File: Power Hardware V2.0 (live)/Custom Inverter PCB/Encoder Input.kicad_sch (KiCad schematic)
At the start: 0 parts

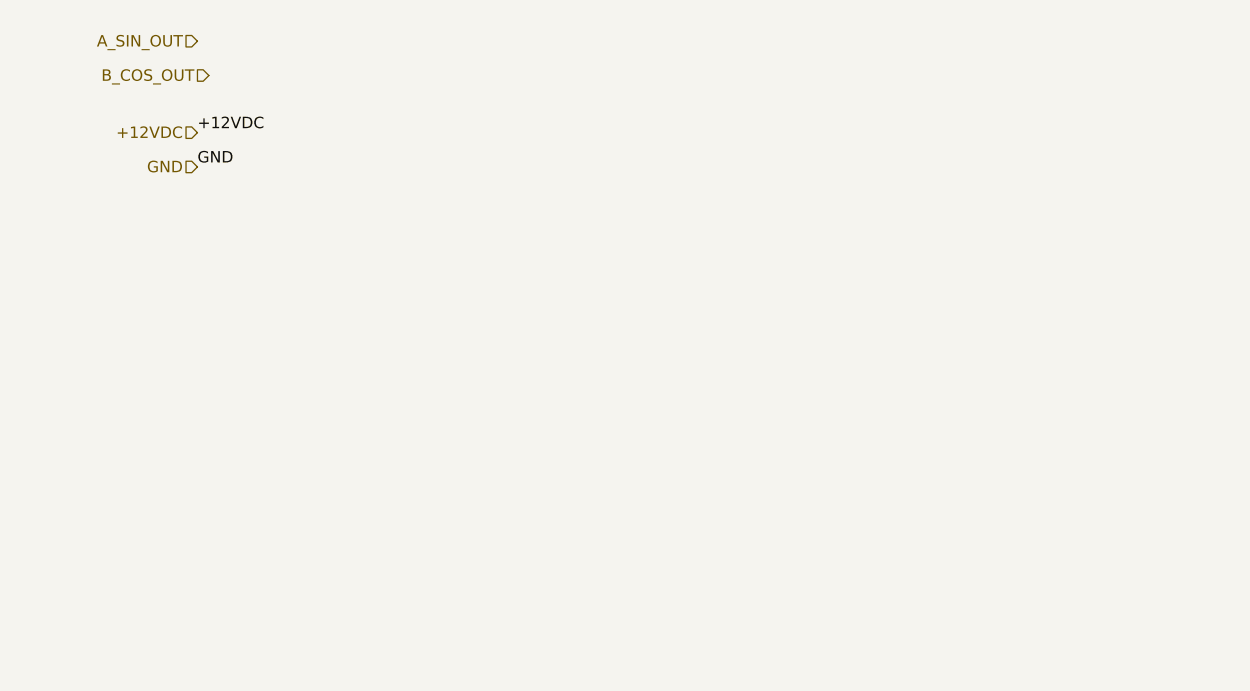
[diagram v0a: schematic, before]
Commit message: Schematic Changes
-Changed 3.3V regulator to a higher power unit for the sin-cos circuit (from 500mA to 3A)
-Fixed flipped MOTA,B,C connection to Output Terminal
- Current Sense IC setup
- Fuses for Phase current outputs
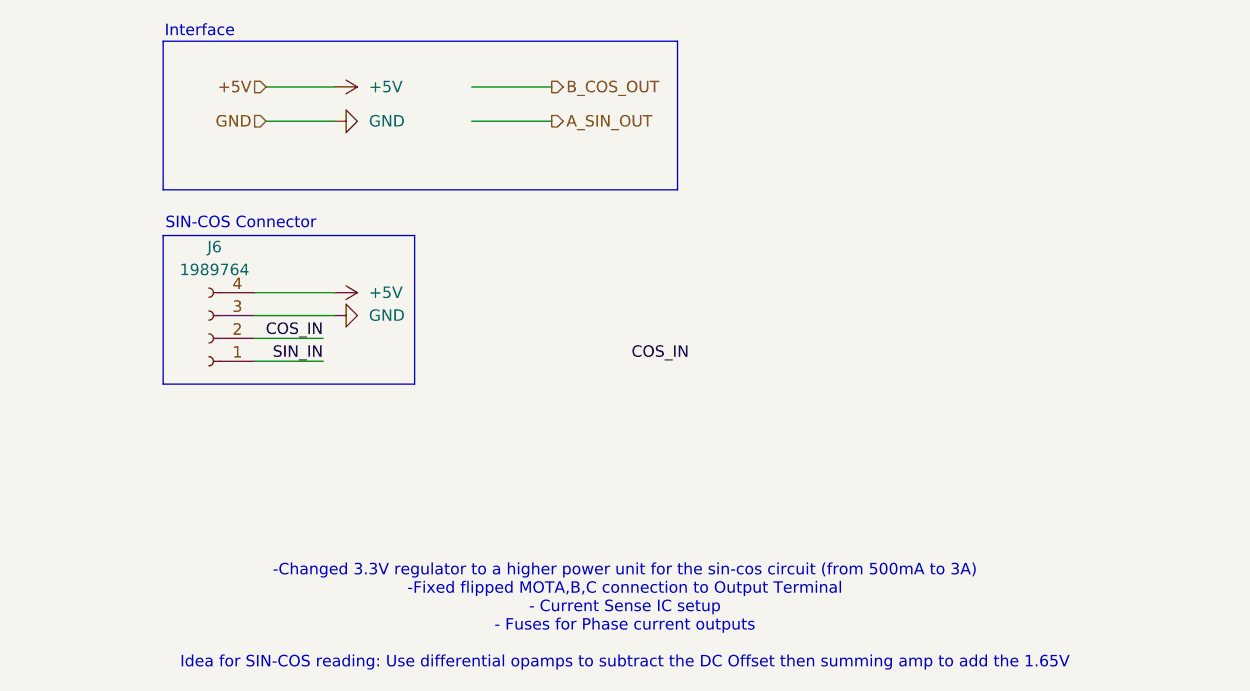
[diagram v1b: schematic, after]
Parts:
- added J6: 1989764, PHOENIX_1989764:PHOENIX_1989764, symbol Connector:Conn_01x04_Socket
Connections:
- net GND: now also J6.3 (Pin_3)
- new net +5V: J6.4 (Pin_4)
- new net COS_IN: J6.2 (Pin_2)
- new net SIN_IN: J6.1 (Pin_1)
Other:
- note added: "-Changed 3.3V regulator to a higher power unit for the sin-cos circuit (from 500mA to 3A) -Fixed flipped MOTA,B,C connection to Output Terminal - Current Sense IC setup - Fuses for Phase current outputs Idea for SIN-COS reading: Use differential opamps to subtract the DC Offset then summing amp to add the 1.65V"
- note added: "Interface"
- note added: "SIN-COS Connector"

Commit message: Sine-cos test
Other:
- note added: "Connection to MCU"
- note added: "Connector To Resolver"
- note removed: "Interface"
- note removed: "SIN-COS Connector"
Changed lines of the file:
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@@
 		)
 	)
-	(text "SIN-COS Connector\n"
+	(text "Connector To Resolver\n"
 		(exclude_from_sim no)
-		(at 30.226 43.18 0)
+		(at 31.496 43.18 0)
 		(effects
 			(font
@@
 	(text "-Changed 3.3V regulator to a higher power unit for the sin-cos circuit (from 500mA to 3A)\n-Fixed flipped MOTA,B,C connection to Output Terminal\n- Current Sense IC setup\n- Fuses for Phase current outputs\n\nIdea for SIN-COS reading: Use differential opamps to subtract the DC Offset then summing amp to add the 1.65V"
 		(exclude_from_sim no)
-		(at 72.898 86.868 0)
+		(at 82.042 108.966 0)
 		(effects
 			(font
@@
 		)
 	)
-	(text "Interface\n"
+	(text "Connection to MCU"
 		(exclude_from_sim no)
-		(at 25.654 21.844 0)
+		(at 30.734 21.844 0)
 		(effects
 			(font
@@
 		)
 	)
+	(label "SIN_IN"
+		(at 78.74 66.04 180)
+		(effects
+			(font
+				(size 1.27 1.27)
+			)
+			(justify right bottom)
+		)
+	)
 	(label "COS_IN"
 		(at 39.37 55.88 180)
@@
 	)
 	(label "COS_IN"
-		(at 80.01 58.42 180)
+		(at 78.74 58.42 180)
 		(effects
 			(font

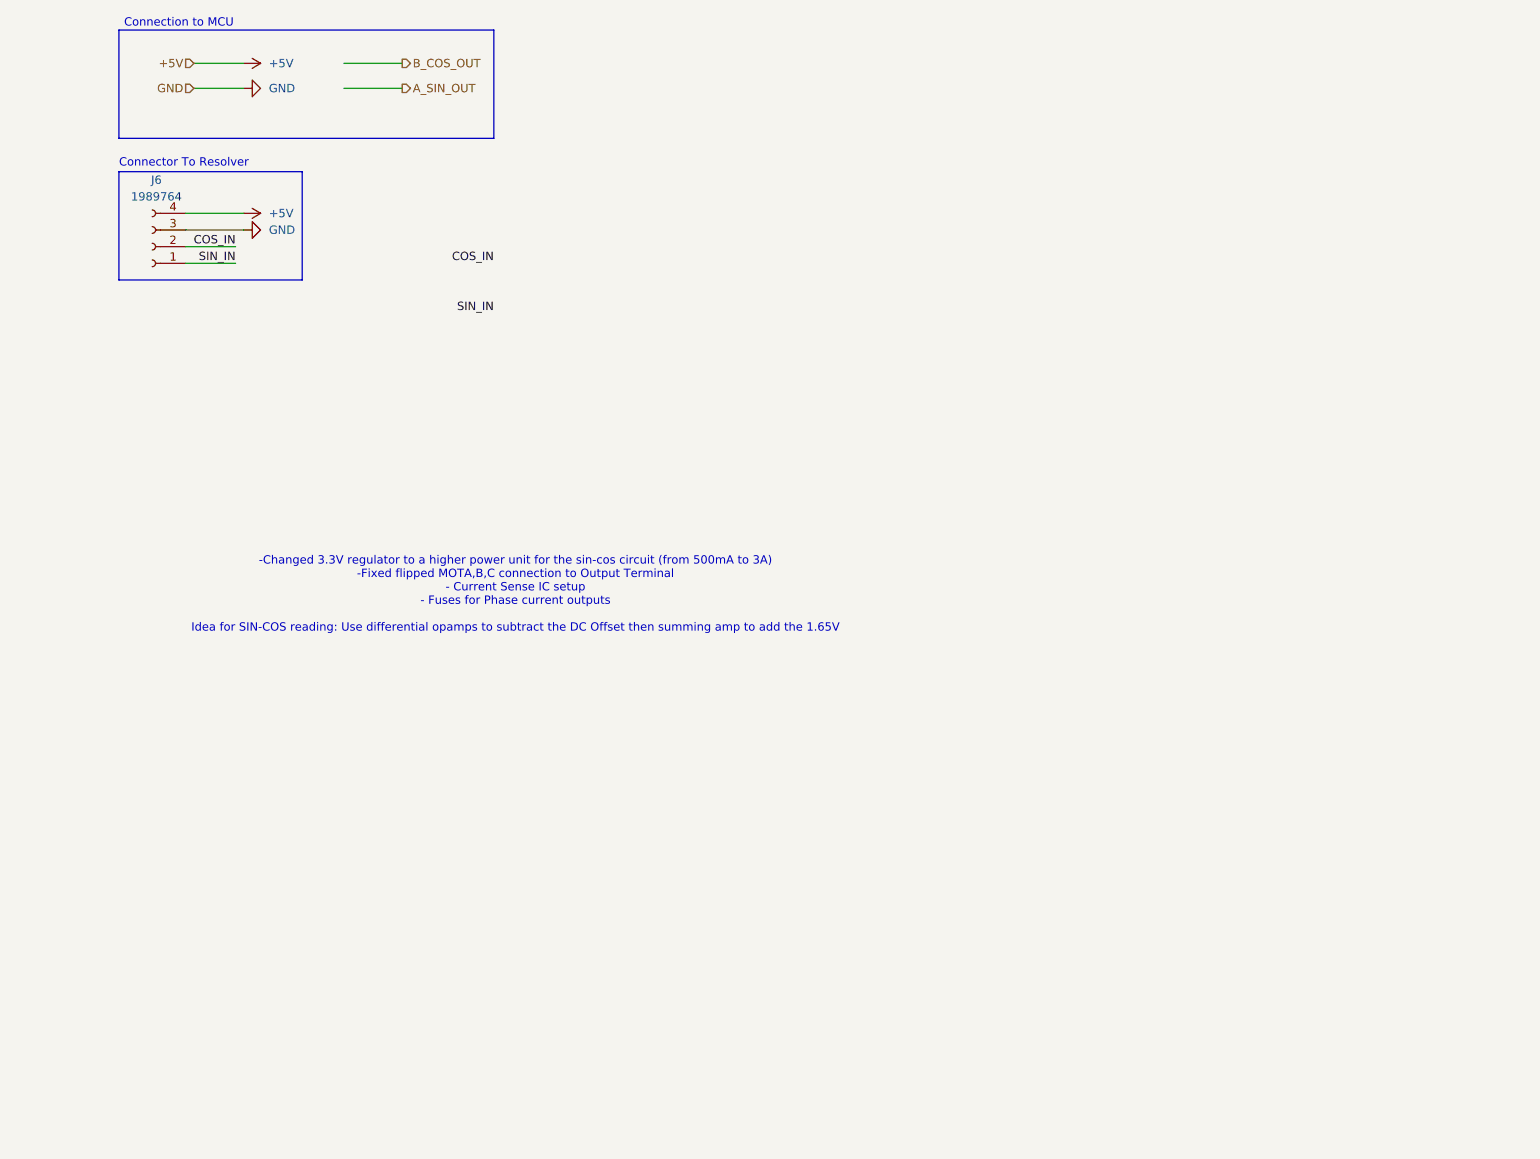
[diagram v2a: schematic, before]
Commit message: Resolver Reading opamps
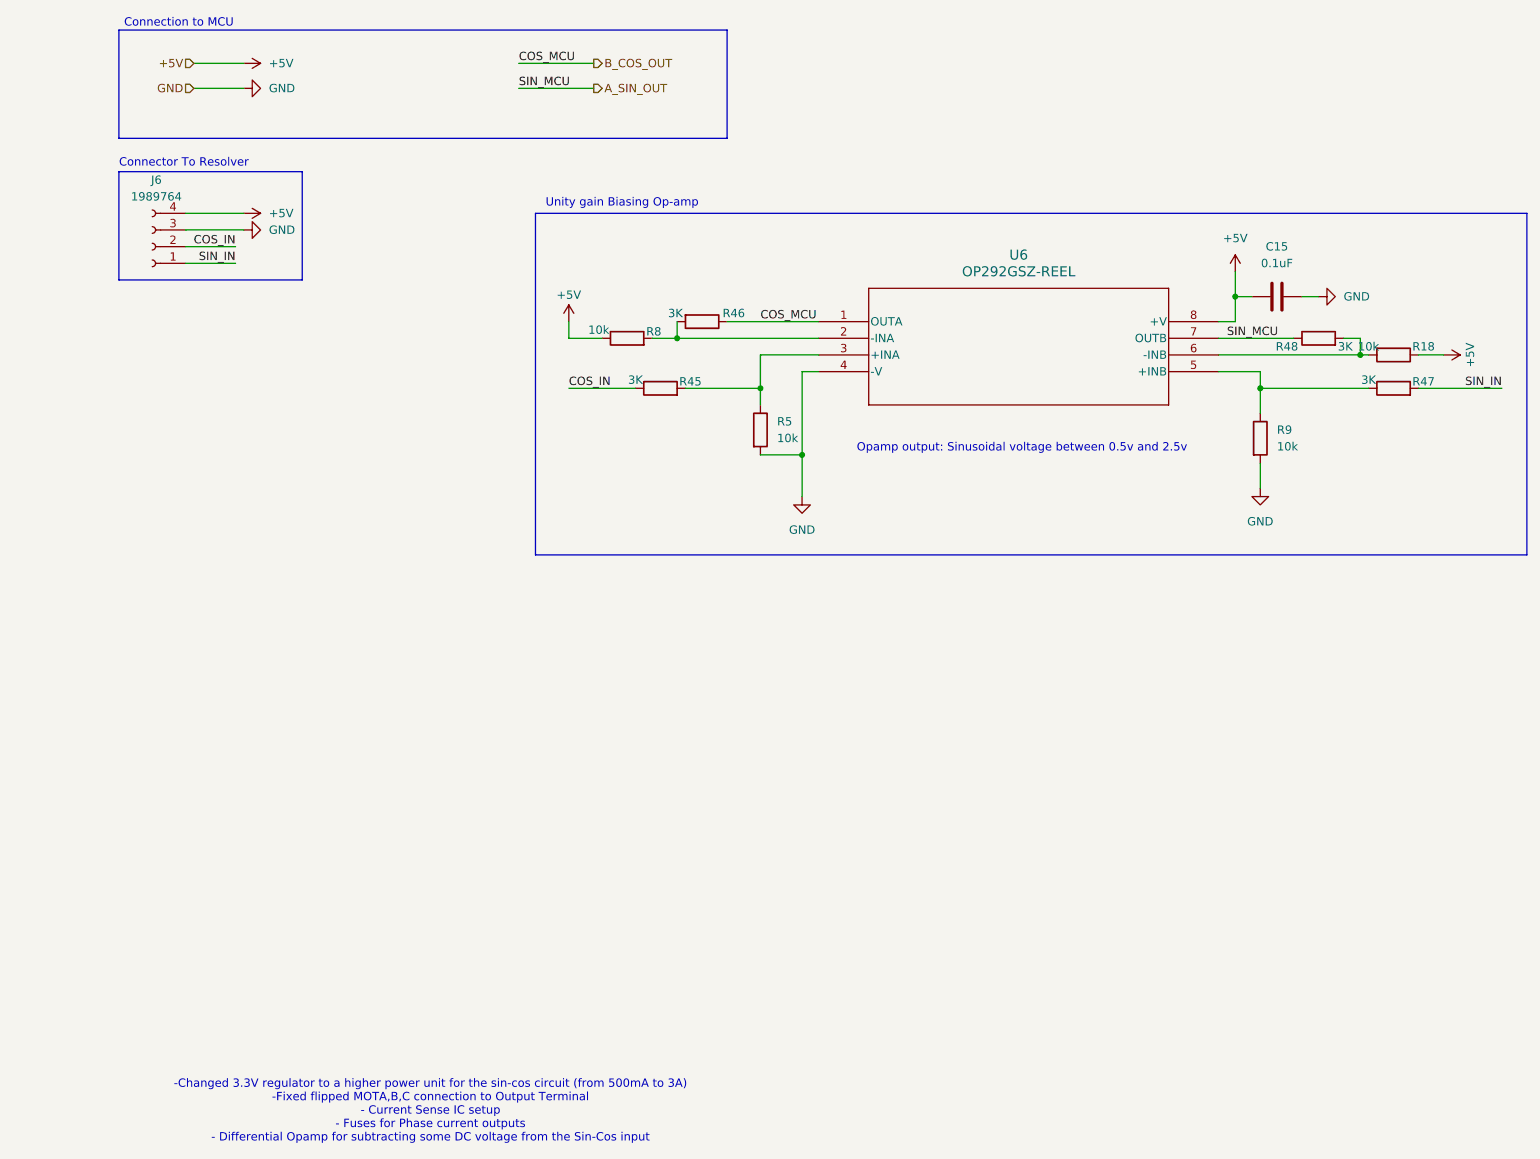
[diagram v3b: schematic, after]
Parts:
- added C15: 0.1uF, Capacitor_SMD:C_0805_2012Metric, symbol Device:C
- added R18, R5, R8, R9: 10k, Resistor_SMD:R_0805_2012Metric, symbol Device:R
- added R45, R46, R47, R48: 3K, Resistor_SMD:R_0805_2012Metric, symbol Device:R
- added U6: OP292GSZ-REEL, R_8_ADI, symbol Opamp:OP292GSZ-REEL
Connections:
- net +5V: now also C15.1, R18.1, R8.1, U6.8 (+V)
- net A_SIN_OUT: now also R48.1, U6.7 (OUTB)
- net B_COS_OUT: now also R46.1, U6.1 (OUTA)
- net COS_IN: now also R45.1
- net GND: now also C15.2, R5.2, R9.2, U6.4 (-V)
- net SIN_IN: now also R47.2
- new net: R46.2, R8.2, U6.2 (-INA)
- new net: R47.1, R9.1, U6.5 (+INB)
- new net: R45.2, R5.1, U6.3 (+INA)
- new net: R18.2, R48.2, U6.6 (-INB)
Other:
- note added: "-Changed 3.3V regulator to a higher power unit for the sin-cos circuit (from 500mA to 3A) -Fixed flipped MOTA,B,C connection to Output Terminal - Current Sense IC setup - Fuses for Phase current outputs - Differential Opamp for subtracting some DC voltage from the Sin-Cos input"
- note added: "Opamp output: Sinusoidal voltage between 0.5v and 2.5v"
- note added: "Unity gain Biasing Op-amp"
- note removed: "-Changed 3.3V regulator to a higher power unit for the sin-cos circuit (from 500mA to 3A) -Fixed flipped MOTA,B,C connection to Output Terminal - Current Sense IC setup - Fuses for Phase current outputs Idea for SIN-COS reading: Use differential opamps to subtract the DC Offset then summing amp to add the 1.65V"
- company: (none) -> M.NGUEN, C.O'BRIEN
- title: (none) -> Resolver Input

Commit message: Pcb layout and tracing
changed footprint file for current sense ic
did layout and tracing for pcb
created bom
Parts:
- R18, R5, R9: Part Number (none) -> ERA-6AEB103V
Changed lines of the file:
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@@
+			)
+		)
+		(property "Part Number" "ERA-6AEB103V"
+			(at 215.9 72.39 0)
+			(effects
+				(font
+					(size 1.27 1.27)
+				)
+				(hide yes)
 			)
 		)
@@
 			)
 		)
+		(property "Part Number" "ERA-6AEB103V"
+			(at 195.58 85.09 0)
+			(effects
+				(font
+					(size 1.27 1.27)
+				)
+				(hide yes)
+			)
+		)
 		(pin "2"
 		)
@@
 			(at 119.38 83.82 0)
 			(effects
+				(font
+					(size 1.27 1.27)
+				)
+				(hide yes)
+			)
+		)
+		(property "Part Number" "ERA-6AEB103V"
+			(at 119.38 83.82 0)
+			(effects
